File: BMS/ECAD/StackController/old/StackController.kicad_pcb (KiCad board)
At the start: 2 copper layers, 85.8 x 62 mm, 209 parts, among them Q1 BC846, Q2 BC846, U1 TLE9012, U2 TMUX1309A, U3 TMUX1309A

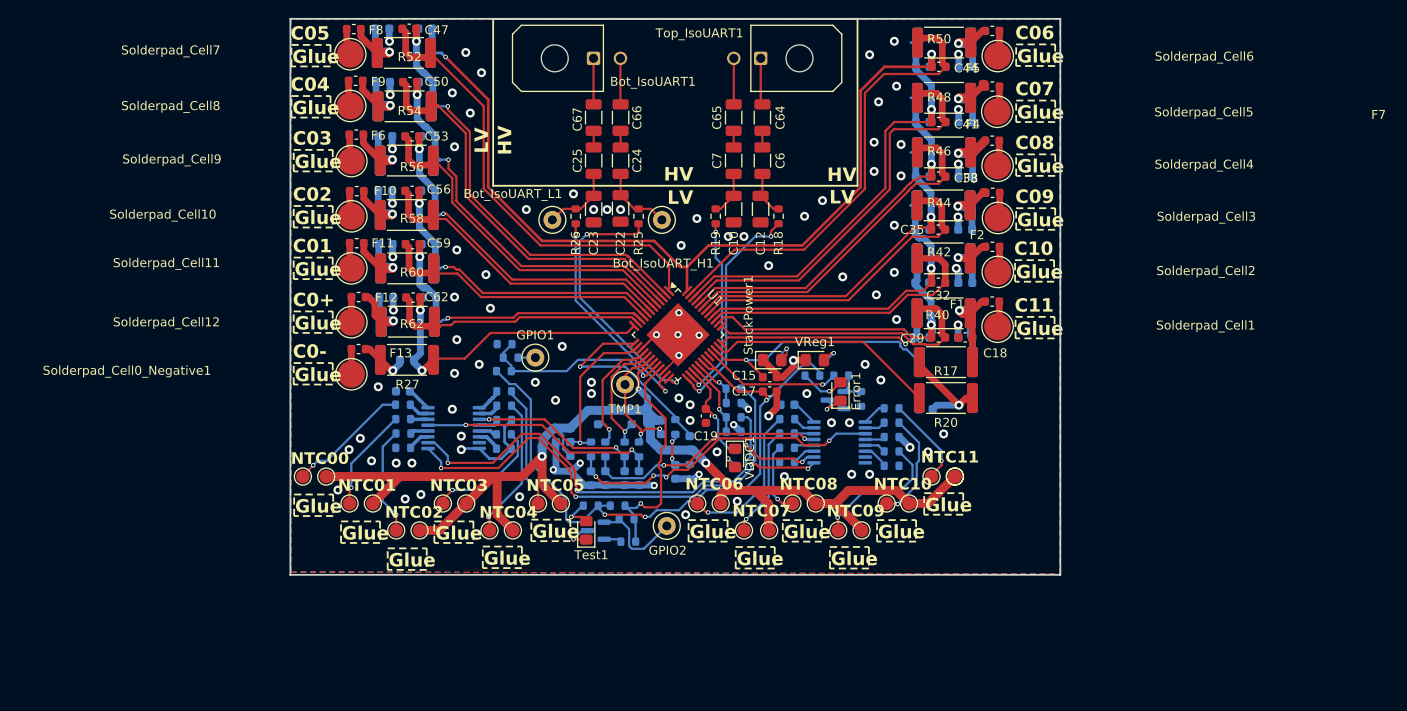
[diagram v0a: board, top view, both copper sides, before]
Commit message: stack controller design close to finished
look into mounting option
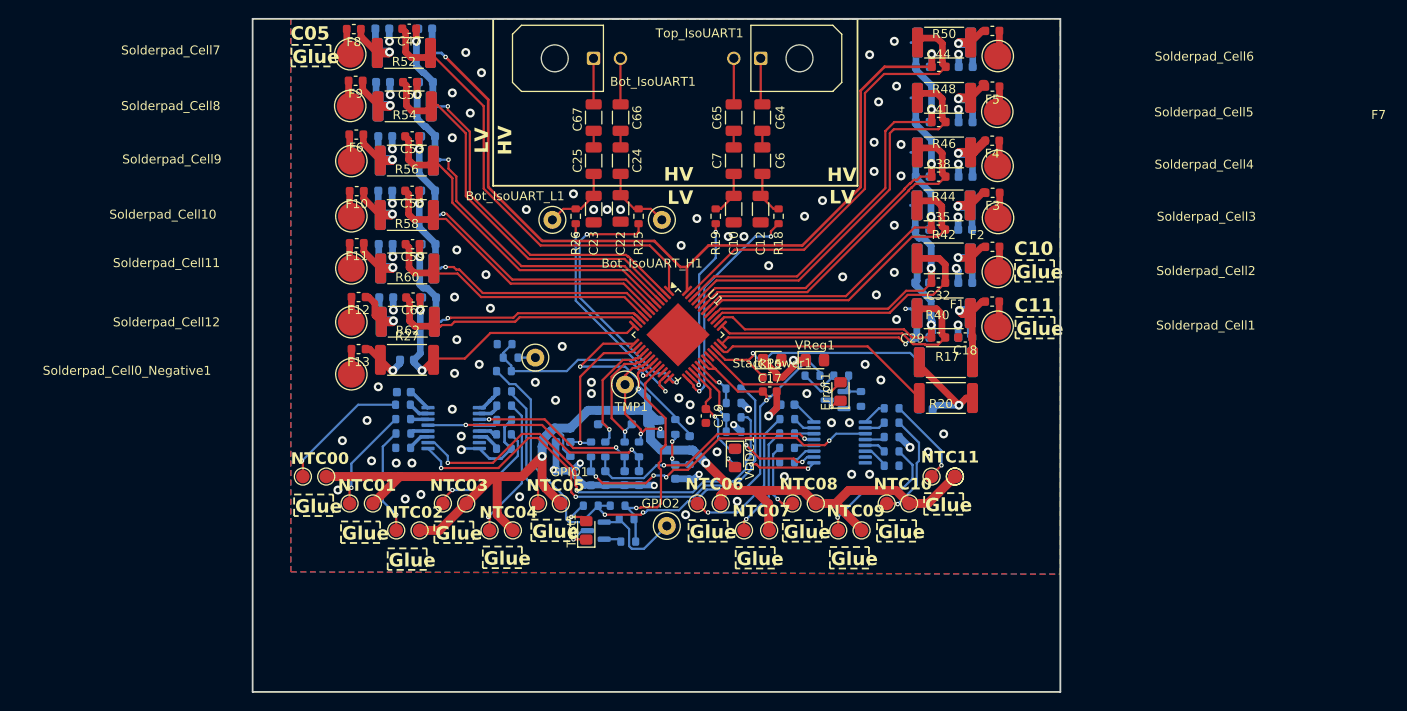
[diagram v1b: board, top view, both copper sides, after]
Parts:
- moved C27 0.14 mm to (28.9, 53.6)
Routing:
- net GND: track 75.7 -> 70.6 mm, vias 98 -> 93
- net Net-(StackPower1-A): track 3.11 -> 0.00 mm, vias 1 -> 0
- net Net-(VReg1-A): track 2.99 -> 0.00 mm, vias 1 -> 0
- net /Balancing_0/U: track 25.2 -> 26.7 mm, vias 1 -> 2
- net NTC02: track 13.7 -> 14.8 mm
- net /Balancing_8/G: track 39.2 -> 40.2 mm
- net Net-(Error1-K): track 3.32 -> 2.26 mm
- net Net-(U1-IFH_L): track 20.8 -> 20.2 mm
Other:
- board size 85.8 x 62 mm -> 90 x 75 mm
- board text removed: "C0+"
- board text removed: "C0-"
- board text removed: "C01"
- board text removed: "C02"
- board text removed: "C03"
- board text removed: "C04"
- board text removed: "C06"
- board text removed: "C07"
- board text removed: "C08"
- board text removed: "C09"
